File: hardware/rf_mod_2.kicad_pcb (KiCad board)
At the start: 4 copper layers, 100 x 100 mm, 184 parts, among them J1001 USB-C, J101 SMA, J102 SMA, J103 SMA, J104 SMA, J1101 SMA, J1102 SMA, J1103 SMA, J201 SMA, J202 SMA, J203 SMA, J204 SMA, J301 SMA, J302 SMA, J303 Pmod, J401 SMA, J402 SMA, J501 SMA, J502 SMA, J503 SMA, J601 SMA, J602 SMA, J701 SMA, J801 SMA, J802 SMA, J901 SMA, J902 SMA, Q101 AO3401A, Q201 AO3401A, Q301 AO3401A, Q401 AO3401A, Q601 AO3401A, Q701 AO3401A, Q702 MMBT3904, Q801 AO3401A, SW101 ON, SW201 ON, SW301 ON, SW401 ON, SW601 ON, SW701 ON, SW801 ON, U1001 LM2664, U101 ADL5375, U1101 SKY13370, U201 ADL5380, U202 OPA810, U203 OPA810, U301 3.3V, U302 MAX2871, U401 QPL9547, U601 AD8318, U701 TPS22917, U702 ADL5611, U801 MAX2659, U802 3.3V

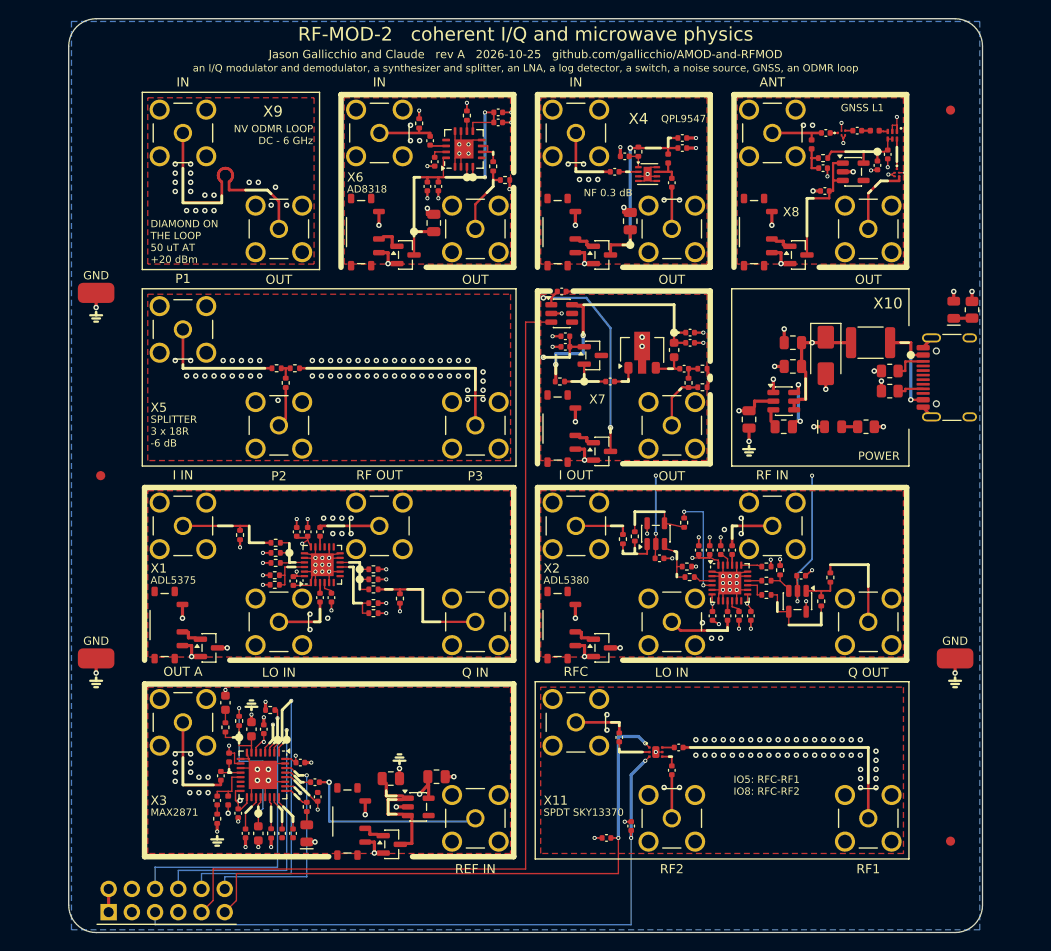
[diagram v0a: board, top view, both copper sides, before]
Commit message: Silkscreen says what each tile is and whose jack is whose: jack names on their own tile's frame, titles in words on the top frame, ranges and levels placed inside; tutorial section numbers off the boards; README tables of every tile (what, chip link, specs, limits, experiments, use, what to buy) and handbook entries as tables with a picture of each tile, both from boards/tile_docs.py
Co-Authored-By: Claude Opus 5.5 <noreply@anthropic.com>
Claude-Session: https://claude.ai/code/session_01RKeoKvFFzjk3cEBLCXXHnB
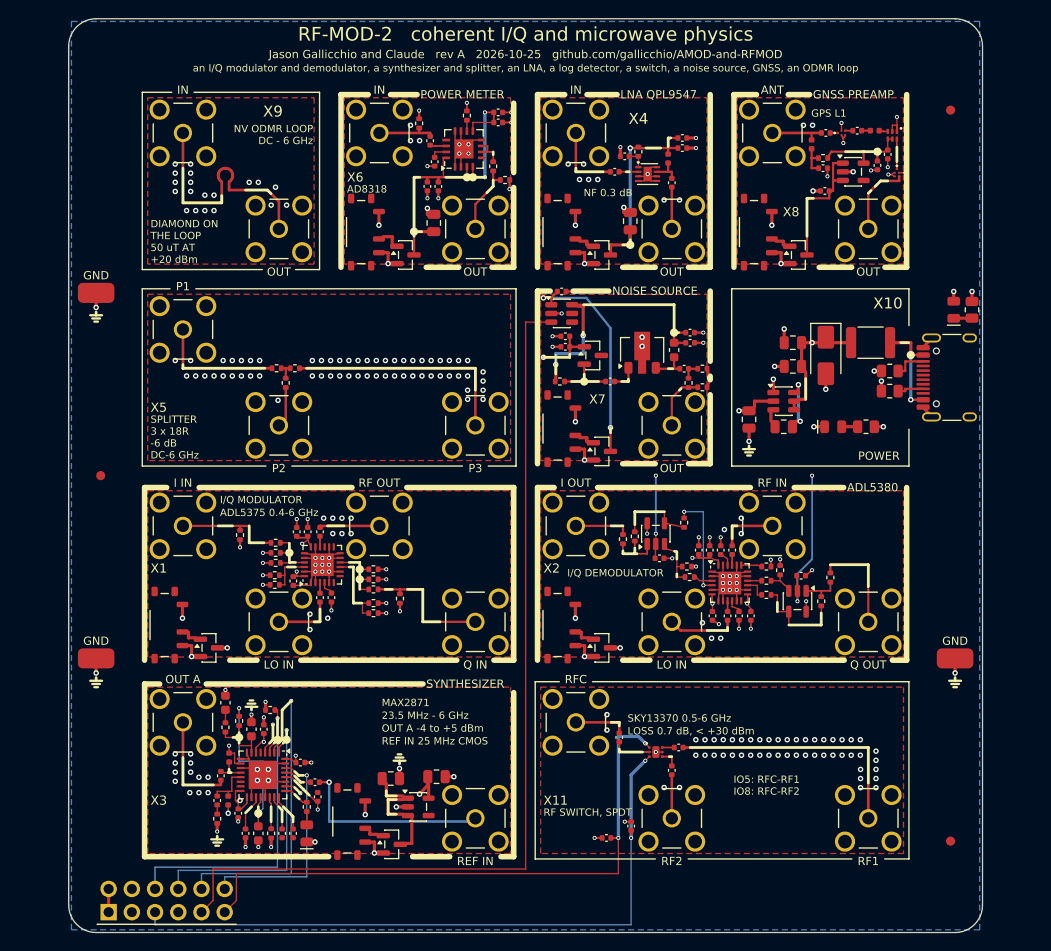
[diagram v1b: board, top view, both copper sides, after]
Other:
- board text added: "23.5 MHz - 6 GHz"
- board text added: "ADL5375 0.4-6 GHz"
- board text added: "DC-6 GHz"
- board text added: "GNSS PREAMP"
- board text added: "GPS L1"
- board text added: "I/Q DEMODULATOR"
- board text added: "I/Q MODULATOR"
- board text added: "LNA QPL9547"
- board text added: "LOSS 0.7 dB, < +30 dBm"
- board text added: "NOISE SOURCE"
- board text added: "OUT A -4 to +5 dBm"
- board text added: "POWER METER"
- board text added: "REF IN 25 MHz CMOS"
- board text added: "RF SWITCH, SPDT"
- board text added: "SKY13370 0.5-6 GHz"
- board text added: "SYNTHESIZER"
- board text removed: "ADL5375"
- board text removed: "GNSS L1"
- board text removed: "QPL9547"
- board text removed: "SPDT SKY13370"

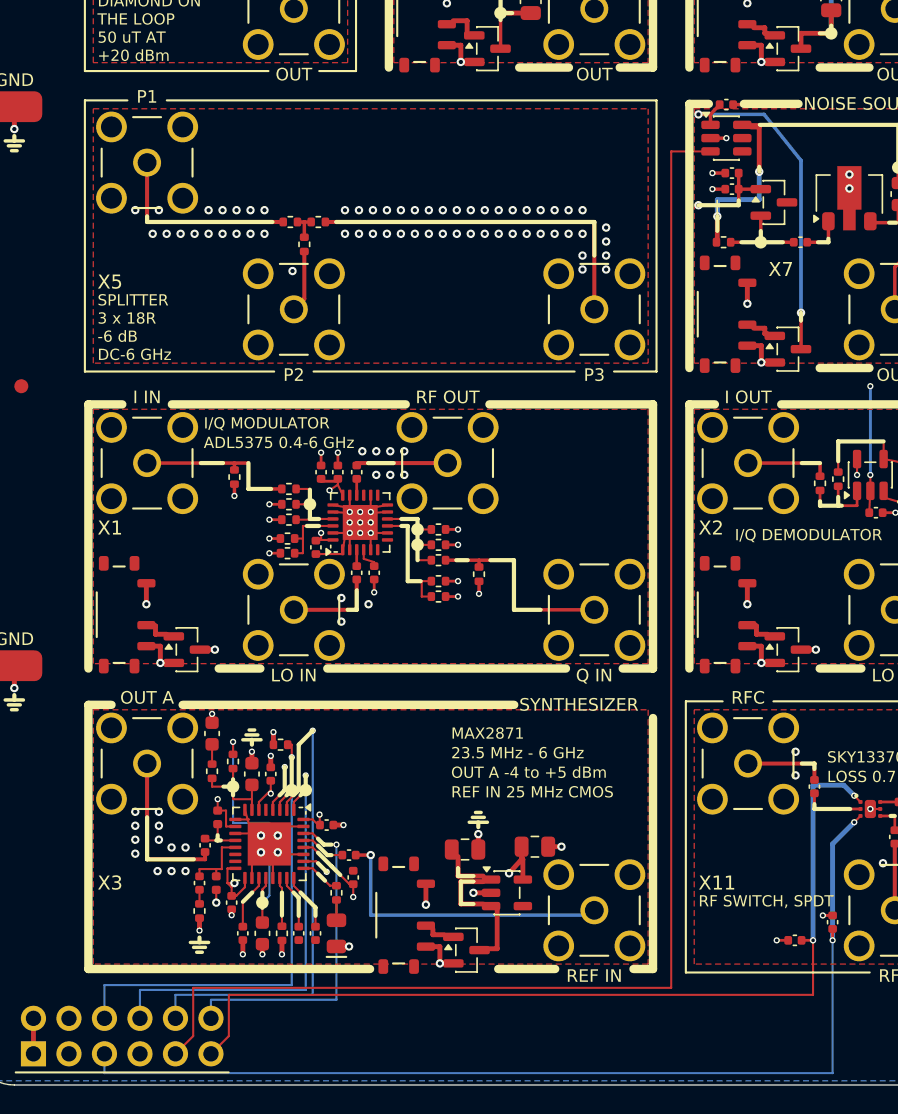
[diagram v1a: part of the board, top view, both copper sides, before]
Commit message: RF-MOD-2: X5 is a dual directional coupler (two HHM22137A1 back to back, 0.6-3.5 GHz, FWD and REFL 25 dB down, 20 dB directivity) in the splitter's place; X3's RFOUTA- on OUT A- (its right cell's bottom-right) so OUT A+ and OUT A- are X1's and X2's LOs, REF IN moved to the right cell's top-left with its line on the back; IO5 and IO6 lowered in the margin under OUT A-'s line
Co-Authored-By: Claude Opus 5.5 <noreply@anthropic.com>
Claude-Session: https://claude.ai/code/session_01RKeoKvFFzjk3cEBLCXXHnB
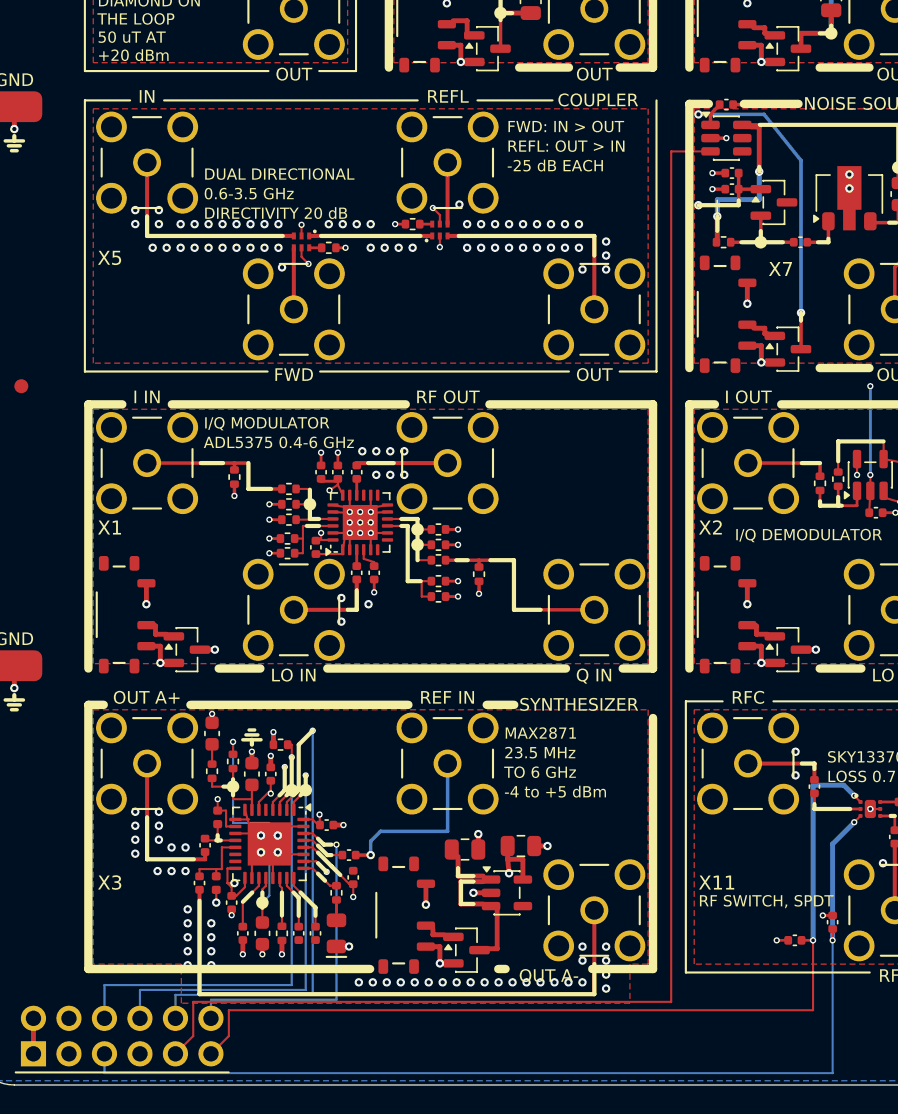
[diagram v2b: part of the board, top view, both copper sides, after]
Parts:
- removed R306: 5.1k, Resistor_SMD:R_0402_1005Metric
- removed R503: 18R, Resistor_SMD:R_0402_1005Metric
- added J304: Pmod, amod:PinHeader_2x06_P2.54mm_Horizontal_PZ254R-12-12P, F.Cu at (10.7, 96.5)
- added J504: SMA, amod:SMA_BWSMA-KE-Z001_Vertical, F.Cu at (44.5, 44.5)
- added U501: HHM22137A1, amod:Coupler_1608-6P_HHM22137A1, F.Cu at (23.6, 39.7)
- added U502: HHM22137A1, amod:Coupler_1608-6P_HHM22137A1, F.Cu at (33.4, 38.8)
- J303: value Pmod -> SMA; footprint amod:PinHeader_2x06_P2.54mm_Horizontal_PZ254R-12-12P -> amod:SMA_BWSMA-KE-Z001_Vertical
- R305: value 51R -> 5.1k
- R501, R502: value 18R -> 51R
- moved J303 35.0 mm to (44.5, 87.5)
- moved J302 14.8 mm to (34.0, 77.0)
- moved J503 14.8 mm to (34.0, 34.0)
- moved R502 6.75 mm to (31.5, 38.4)
- moved R305 6.11 mm to (22.1, 89.2)
- moved R501 3.31 mm to (25.5, 40.1)
- moved C302 1.00 mm to (39.2, 82.9)
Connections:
- C310 pad 2: /X3_TRM -> /X3_OUTAN
- J303 pad 1: /PMOD_VCC -> /X3_OUTAN
- J303 pad 2: /PMOD_VCC -> GND
- J501 pad 1: /X5_P1 -> /X5_IN
- J502 pad 1: /X5_P2 -> /X5_FWD
- J503 pad 1: /X5_P3 -> /X5_REFL
- R305 pad 1: /X3_TRM -> /X3_RS
- R501 pad 1: /X5_P1 -> /X5_TA
- R501 pad 2: /X5_N -> GND
- R502 pad 1: /X5_N -> GND
- R502 pad 2: /X5_P3 -> /X5_TB
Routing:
- net /X3_OUTAN: track 0.00 -> 41.7 mm
- net /X5_P3: track 25.5 -> 0.00 mm
- net /X5_OUT: track 0.00 -> 15.8 mm
- net /X5_IN: track 0.00 -> 15.8 mm
- net /X5_P1: track 14.0 -> 0.00 mm
- net /X3_REF: track 21.5 -> 12.7 mm
- net /X5_MID: track 0.00 -> 8.80 mm
- net GND: track 156.4 -> 161.3 mm, vias 282 -> 314
- net /X5_P2: track 4.45 -> 0.00 mm
- net /X5_REFL: track 0.00 -> 4.40 mm
- net /X5_FWD: track 0.00 -> 4.40 mm
- net /X5_N: track 2.07 -> 0.00 mm
- net /X3_TRM: track 1.01 -> 0.00 mm
- net /X5_TB: track 0.00 -> 0.89 mm
- net /X5_TA: track 0.00 -> 0.89 mm
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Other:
- board text added: "-25 dB EACH"
- board text added: "-4 to +5 dBm"
- board text added: "0.6-3.5 GHz"
- board text added: "23.5 MHz"
- board text added: "COUPLER"
- board text added: "DIRECTIVITY 20 dB"
- board text added: "DUAL DIRECTIONAL"
- board text added: "FWD"
- board text added: "FWD: IN > OUT"
- board text added: "OUT A+"
- board text added: "OUT A-"
- board text added: "REFL"
- board text added: "REFL: OUT > IN"
- board text added: "TO 6 GHz"
- board text added: "at RF; X3's OUT A+ and A- are their LOs. Jacks at each"
- board text removed: "-6 dB"
- board text removed: "23.5 MHz - 6 GHz"
- board text removed: "3 x 18R"
- board text removed: "DC-6 GHz"
- board text removed: "OUT A"
- board text removed: "OUT A -4 to +5 dBm"
- board text removed: "P1"
- board text removed: "P2"
- board text removed: "P3"
- board text removed: "REF IN 25 MHz CMOS"
- board text removed: "SPLITTER"
- board text removed: "at RF; X3 split by X5 is the LO of both. Jacks at each"

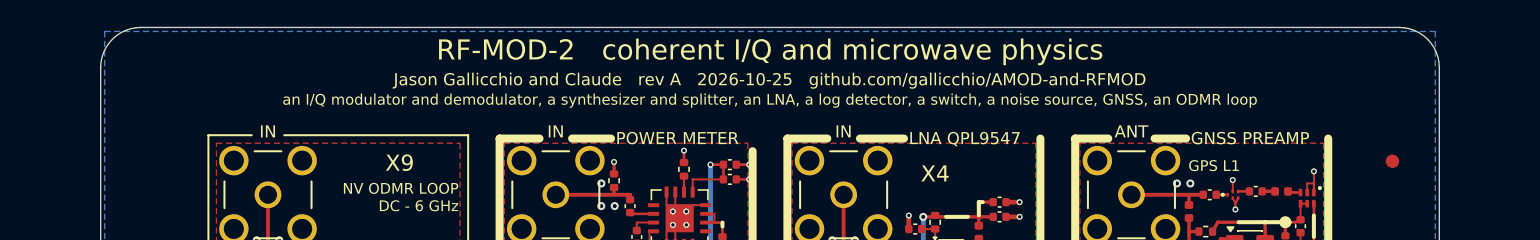
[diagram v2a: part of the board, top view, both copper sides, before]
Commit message: RF-MOD and RF-MOD-2 subtitles (on the copper and the schematic) without the splitters; rebuilt
Co-Authored-By: Claude Opus 5.5 <noreply@anthropic.com>
Claude-Session: https://claude.ai/code/session_01RKeoKvFFzjk3cEBLCXXHnB
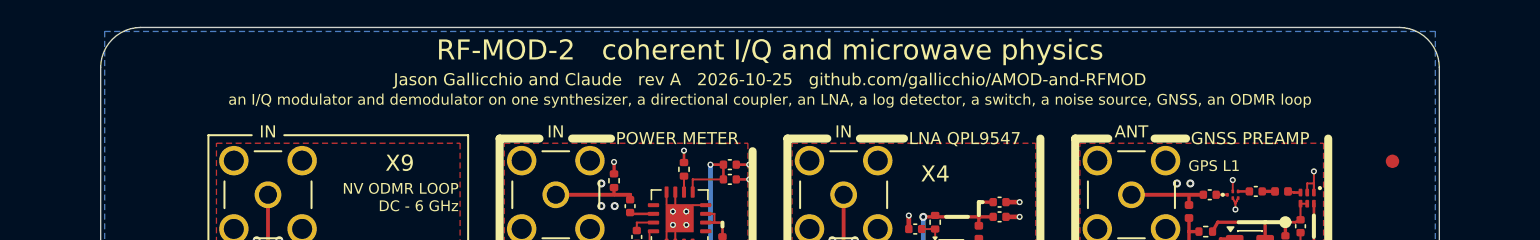
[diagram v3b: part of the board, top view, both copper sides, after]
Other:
- board text added: "an I/Q modulator and demodulator on one synthesizer, a directional coupler, an LNA, a log detector, a switch, a noise source, GNSS, an ODMR loop"
- board text removed: "an I/Q modulator and demodulator, a synthesizer and splitter, an LNA, a log detector, a switch, a noise source, GNSS, an ODMR loop"
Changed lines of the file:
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@@
 		)
 	)
-	(gr_text "an I/Q modulator and demodulator, a synthesizer and splitter, an LNA, a log detector, a switch, a noise source, GNSS, an ODMR loop"
+	(gr_text "an I/Q modulator and demodulator on one synthesizer, a directional coupler, an LNA, a log detector, a switch, a noise source, GNSS, an ODMR loop"
 		(at 50 5.4 0)
 		(layer "F.SilkS")

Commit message: Silk case convention on all six boards (Jason, Prompt 17: "To distinguish whole-tile labels from SMA or port labels, use different cases")
Ports (the jacks' names, terminal and loop names, a port named inside a note) stay UPPER CASE.  A tile's label (its
title on the frame, its name in the corner) is Mixed case: the first letter capitalised and the rest as written ("RC
low-pass", "Synthesizer", "I/Q demodulator"; tiles.label_case).  Ranges, values and notes are lower case except units,
acronyms and part numbers ("loss 1.7 dB", "OUT floats").  RF-MOD-2's X1 and X2 take word titles with their chips in
the info; RF-MOD's and RF-MOD-2's LNA tiles are titled "Preamp" ("Low-noise amp" does not fit a cell's frame); a few
two-line labels moved 0.15-0.3 mm for the descenders mixed case brings.  AMOD-P2's tile records (tile_docs), its DOA
list, KIT.md's AMOD-P2 section; X5's calibration points at P14.  All six boards: ERC 0, DRC 0, all fab checks.

Co-Authored-By: Claude Opus 5.5 <noreply@anthropic.com>
Claude-Session: https://claude.ai/code/session_01RKeoKvFFzjk3cEBLCXXHnB
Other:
- board text added: "-25 dB each"
- board text added: "50 uT at"
- board text added: "ADL5380 0.4-6 GHz"
- board text added: "Coupler"
- board text added: "GNSS preamp"
- board text added: "I/Q demodulator"
- board text added: "I/Q modulator"
- board text added: "NV ODMR loop"
- board text added: "Noise source"
- board text added: "Power"
- board text added: "Power meter"
- board text added: "Preamp"
- board text added: "RF switch, SPDT"
- board text added: "Synthesizer"
- board text added: "diamond on"
- board text added: "directivity 20 dB"
- board text added: "dual directional"
- board text added: "loss 0.7 dB, < +30 dBm"
- board text added: "the loop"
- board text added: "to 6 GHz"
- board text removed: "-25 dB EACH"
- board text removed: "50 uT AT"
- board text removed: "ADL5380"
- board text removed: "COUPLER"
- board text removed: "DIAMOND ON"
- board text removed: "DIRECTIVITY 20 dB"
- board text removed: "DUAL DIRECTIONAL"
- board text removed: "GNSS PREAMP"
- board text removed: "I/Q DEMODULATOR"
- board text removed: "I/Q MODULATOR"
- board text removed: "LNA QPL9547"
- board text removed: "LOSS 0.7 dB, < +30 dBm"
- board text removed: "NOISE SOURCE"
- board text removed: "NV ODMR LOOP"
- board text removed: "POWER"
- board text removed: "POWER METER"
- board text removed: "RF SWITCH, SPDT"
- board text removed: "SYNTHESIZER"
- board text removed: "THE LOOP"
- board text removed: "TO 6 GHz"
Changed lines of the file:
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@@
 	(gr_line
 		(start 35.215714 8.3)
-		(end 38.125715 8.3)
+		(end 39.154284 8.3)
 		(stroke
 			(width 0.6)
@@
 	(gr_line
 		(start 36.137143 29.55)
-		(end 41.511428 29.55)
+		(end 42.497141 29.55)
 		(stroke
 			(width 0.15)
@@
 	(gr_line
 		(start 36.801429 72.8)
-		(end 38.768571 72.8)
+		(end 39.968571 72.8)
 		(stroke
 			(width 0.6)
@@
 	(gr_line
 		(start 36.994286 51.3)
-		(end 48.7 51.3)
+		(end 37.825713 51.3)
 		(stroke
 			(width 0.6)
@@
 	)
 	(gr_line
-		(start 48.7 9.2424)
+		(start 48.7 8.3)
 		(end 48.7 16.835)
 		(stroke
@@
 	)
 	(gr_line
-		(start 48.7 51.3)
+		(start 48.7 52.2424)
 		(end 48.7 70.2)
 		(stroke
@@
 	(gr_line
 		(start 55.205 29.8)
-		(end 59.111428 29.8)
+		(end 60.311427 29.8)
 		(stroke
 			(width 0.6)
@@
 	(gr_line
 		(start 56.715714 8.3)
-		(end 60.011428 8.3)
+		(end 64.082855 8.3)
 		(stroke
 			(width 0.6)
@@
 	(gr_line
 		(start 57.872857 51.3)
-		(end 74.605715 51.3)
+		(end 60.989997 51.3)
 		(stroke
 			(width 0.6)
@@
 	)
 	(gr_line
+		(start 73.449999 51.3)
+		(end 74.605715 51.3)
+		(stroke
+			(width 0.6)
+			(type default)
+		)
+		(layer "F.SilkS")
+	)
+	(gr_line
 		(start 74.45 46.75)
 		(end 74.45 47.1)
@@
 	(gr_line
 		(start 78.729999 8.3)
-		(end 81.082857 8.3)
+		(end 81.425713 8.3)
 		(stroke
 			(width 0.6)
@@
 	(gr_line
 		(start 79.394286 51.3)
-		(end 84.811428 51.3)
+		(end 91.7 51.3)
 		(stroke
 			(width 0.6)
@@
 		(layer "Edge.Cuts")
 	)
-	(gr_text "DIAMOND ON"
-		(at 8.95 22.45 0)
+	(gr_text "dual directional"
+		(at 8.549999 42.85 0)
 		(layer "F.SilkS")
 		(effects
@@
 		)
 	)
-	(gr_text "THE LOOP"
-		(at 8.95 23.75 0)
-		(layer "F.SilkS")
-		(effects
-			(font
-				(size 0.8 0.8)
-				(thickness 0.15)
-			)
-			(justify left)
-		)
-	)
-	(gr_text "50 uT AT"
-		(at 8.95 25.05 0)
+	(gr_text "0.6-3.5 GHz"
+		(at 8.549999 44.25 0)
 		(layer "F.SilkS")
 		(effects
@@
 		)
 	)
-	(gr_text "+20 dBm"
-		(at 8.95 26.35 0)
+	(gr_text "directivity 20 dB"
+		(at 8.549999 45.65 0)
 		(layer "F.SilkS")
 		(effects
@@
 		)
 	)
-	(gr_text "DUAL DIRECTIONAL"
-		(at 16.55 34.85 0)
+	(gr_text "diamond on"
+		(at 8.95 22.45 0)
 		(layer "F.SilkS")
 		(effects
@@
 		)
 	)
-	(gr_text "0.6-3.5 GHz"
-		(at 16.55 36.25 0)
+	(gr_text "the loop"
+		(at 8.95 23.75 0)
 		(layer "F.SilkS")
 		(effects
@@
 		)
 	)
-	(gr_text "DIRECTIVITY 20 dB"
-		(at 16.55 37.65 0)
+	(gr_text "50 uT at"
+		(at 8.95 25.05 0)
 		(layer "F.SilkS")
 		(effects
@@
 		)
 	)
-	(gr_text "I/Q MODULATOR"
-		(at 16.55 52.65 0)
+	(gr_text "+20 dBm"
+		(at 8.95 26.35 0)
 		(layer "F.SilkS")
 		(effects
@@
 		)
 	)
-	(gr_text "TO 6 GHz"
+	(gr_text "to 6 GHz"
 		(at 38.05 77.649999 0)
 		(layer "F.SilkS")
@@
 		)
 	)
-	(gr_text "-25 dB EACH"
+	(gr_text "-25 dB each"
 		(at 38.25 34.25 0)
 		(layer "F.SilkS")
@@
 		)
 	)
-	(gr_text "RF SWITCH, SPDT"
+	(gr_text "RF switch, SPDT"
 		(at 51.95 86.85 0)
 		(layer "F.SilkS")
@@
 		)
 	)
-	(gr_text "I/Q DEMODULATOR"
-		(at 54.55 60.65 0)
+	(gr_text "NF 0.3 dB"
+		(at 56.35 19.05 0)
 		(layer "F.SilkS")
 		(effects
@@
 		)
 	)
-	(gr_text "NF 0.3 dB"
-		(at 56.35 19.05 0)
+	(gr_text "SKY13370 0.5-6 GHz"
+		(at 61.15 76.55 0)
 		(layer "F.SilkS")
 		(effects
@@
 		)
 	)
-	(gr_text "SKY13370 0.5-6 GHz"
-		(at 61.15 76.55 0)
+	(gr_text "loss 0.7 dB, < +30 dBm"
+		(at 61.15 77.95 0)
 		(layer "F.SilkS")
 		(effects
@@
 		)
 	)
-	(gr_text "LOSS 0.7 dB, < +30 dBm"
-		(at 61.15 77.95 0)
+	(gr_text "ADL5380 0.4-6 GHz"
+		(at 69.95 68.25 0)
 		(layer "F.SilkS")
 		(effects
@@
 		)
 	)
-	(gr_text "NV ODMR LOOP"
+	(gr_text "NV ODMR loop"
 		(at 26.75 12.05 0)
 		(layer "F.SilkS")
@@
 		)
 	)
-	(gr_text "POWER"
+	(gr_text "Power"
 		(at 90.95 47.85 0)
 		(layer "F.SilkS")
@@
 		)
 	)
-	(gr_text "POWER METER"
-		(at 38.475715 8.3 0)
+	(gr_text "I/Q modulator"
+		(at 38.175713 51.3 0)
+		(layer "F.SilkS")
+		(effects
+			(font
+				(size 0.9 0.9)
+				(thickness 0.18)
+			)
+			(justify left)
+		)
+	)
+	(gr_text "Power meter"
+		(at 39.504284 8.3 0)
 		(layer "F.SilkS")
 		(effects
@@
 		)
 	)
-	(gr_text "SYNTHESIZER"
-		(at 39.118571 72.8 0)
+	(gr_text "Synthesizer"
+		(at 40.318571 72.8 0)
 		(layer "F.SilkS")
 		(effects
@@
 		)
 	)
-	(gr_text "COUPLER"
-		(at 41.861429 29.55 0)
+	(gr_text "Coupler"
+		(at 42.847141 29.55 0)
 		(layer "F.SilkS")
 		(effects
@@
 		)
 	)
-	(gr_text "NOISE SOURCE"
-		(at 59.461428 29.8 0)
+	(gr_text "Noise source"
+		(at 60.661427 29.8 0)
 		(layer "F.SilkS")
 		(effects
@@
 		)
 	)
-	(gr_text "LNA QPL9547"
-		(at 60.361428 8.3 0)
+	(gr_text "I/Q demodulator"
+		(at 61.339997 51.3 0)
 		(layer "F.SilkS")
 		(effects
@@
 		)
 	)
-	(gr_text "GNSS PREAMP"
-		(at 81.432857 8.3 0)
+	(gr_text "Preamp"
+		(at 64.432855 8.3 0)
 		(layer "F.SilkS")
 		(effects
@@
 		)
 	)
-	(gr_text "ADL5380"
-		(at 85.161428 51.3 0)
+	(gr_text "GNSS preamp"
+		(at 81.775713 8.3 0)
 		(layer "F.SilkS")
 		(effects
